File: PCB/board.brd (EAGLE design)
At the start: 160 x 100 mm, 24 parts, among them J1 DCJ0202, Q1 CRYSTAL_16MHZ_SMD, U1 MLX90614_

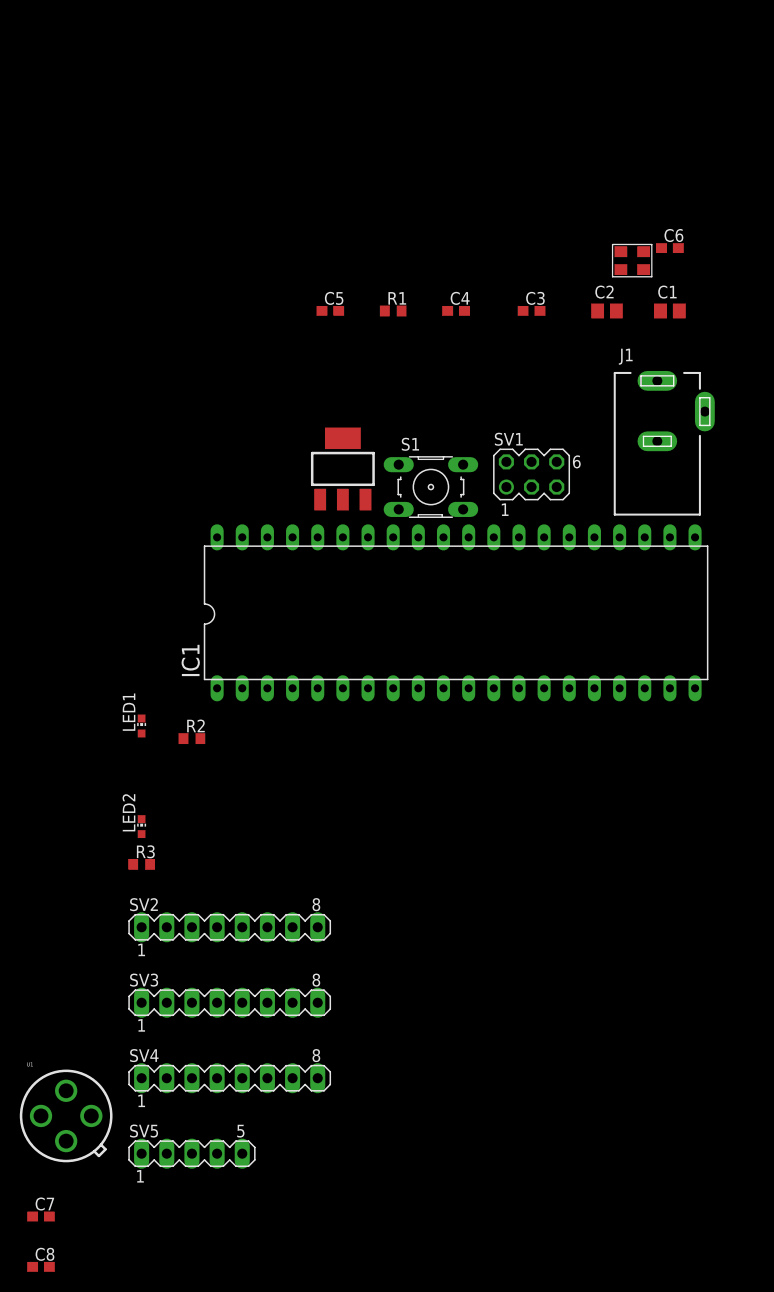
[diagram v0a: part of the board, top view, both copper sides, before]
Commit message: updated PCB with new LDO and PCB footprint
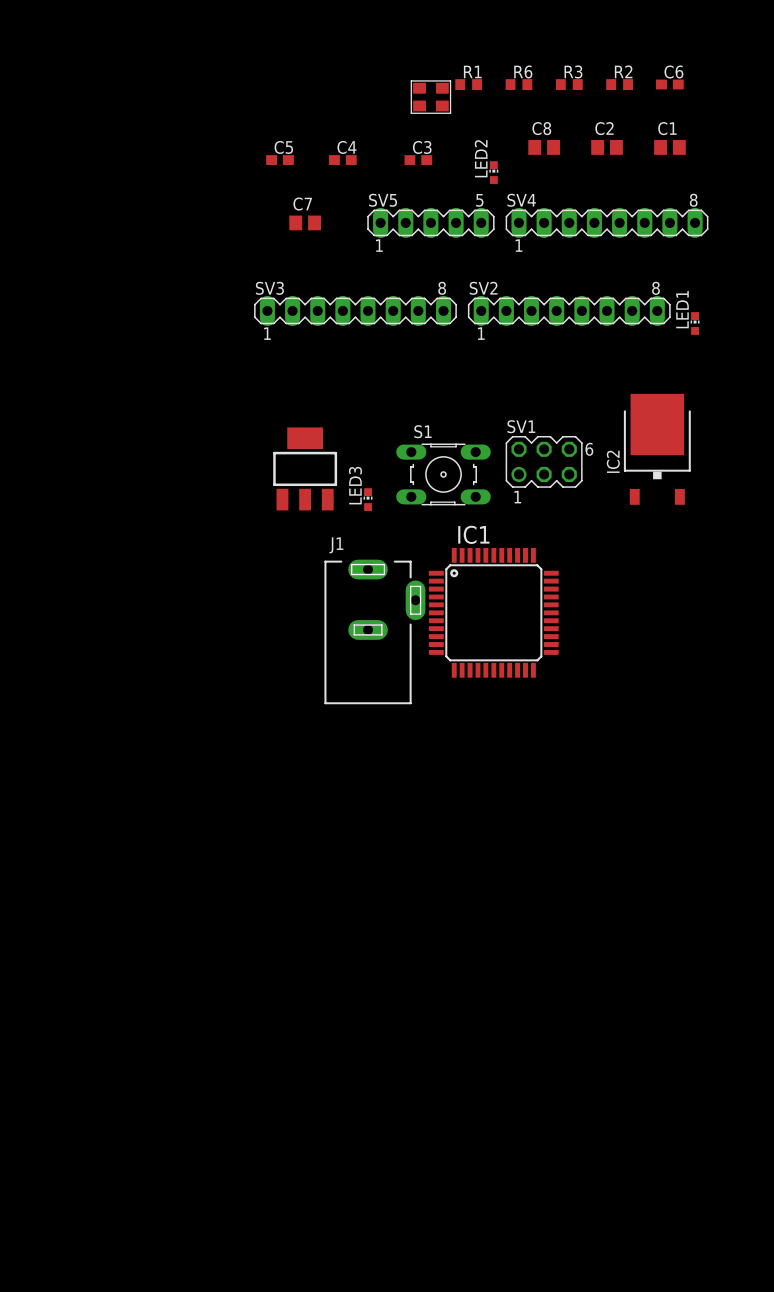
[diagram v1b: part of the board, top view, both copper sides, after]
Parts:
- removed U1: MLX90614_, SparkFun:TO-39
- added IC2: MC33269D-3.3, linear:DPACK
- added LED3: YELLOW, led:CHIP-LED0603
- added R6: 150, rcl:R0603
- C7: value 10pF -> 0.33uF; device rcl:C0603 -> rcl:C0805
- C8: value 10pF -> 10uF; device rcl:C0603 -> rcl:C0805
- IC1: value (none) -> MEGA1284P-SQUARE; device 1284p:DIL40 -> 1284p:TQFP44
- R1: value 10k Ohms -> 10k
- R2, R3: value 150 Ohms -> 150
- moved C8 123.9 mm to (-30.5, 57.1)
- moved C7 103.8 mm to (-54.6, 49.5)
- moved SV5 97.0 mm to (-41.9, 49.5)
- moved SV4 94.4 mm to (-24.1, 49.5)
- moved R3 89.8 mm to (-27.9, 63.5)
- moved R2 78.9 mm to (-22.9, 63.5)
- moved LED2 75.0 mm to (-35.6, 54.6)
- moved SV2 71.1 mm to (-27.9, 40.6)
- moved SV3 71.0 mm to (-49.5, 40.6)
- moved LED1 69.1 mm to (-15.2, 39.4)
- moved J1 34.9 mm to (-48.3, 11.4)
- moved Q1 26.2 mm to (-41.9, 62.2)
- moved R1 24.1 mm to (-38.1, 63.5)
- moved C3 19.1 mm to (-43.2, 55.9)
- moved C4 19.1 mm to (-50.8, 55.9)
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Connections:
- new net N$37: LED3.A, R6.1
- net +3V3: now also C8.1, IC2.2, R6.2; no longer U1.3
- net +5V: now also C7.1, IC1.27, IC1.5, IC2.3; no longer IC1.10, IC1.30
- net GND: now also C7.2, IC1.28, IC1.6, IC2.1, LED3.C; no longer C7.1, IC1.11, IC1.31, U1.4
- net MISO: now also IC1.2; no longer IC1.7
- net MOSI: now also IC1.1; no longer IC1.6
- net N$10: now also IC1.13; no longer IC1.18
- net N$11: now also IC1.12; no longer IC1.17
- net N$12: now also IC1.11; no longer IC1.16
- net N$13: now also IC1.10; no longer IC1.15
- net N$14: now also IC1.9; no longer IC1.14
- net N$15: now also IC1.26; no longer IC1.29
- net N$16: now also IC1.25; no longer IC1.28
- net N$17: now also IC1.24; no longer IC1.27
- net N$18: now also IC1.23; no longer IC1.26
- net N$19: now also IC1.22; no longer IC1.25
- net N$2: now also IC1.29; no longer IC1.32
- net N$20: now also IC1.21; no longer IC1.24
- net N$23: now also IC1.37; no longer IC1.40
- net N$24: now also IC1.36; no longer IC1.39
- net N$25: now also IC1.35; no longer IC1.38
- net N$26: now also IC1.34; no longer IC1.37
- net N$27: now also IC1.33; no longer IC1.36
- net N$28: now also IC1.32; no longer IC1.35
- net N$29: now also IC1.31; no longer IC1.34
- net N$3: now also IC1.8; no longer IC1.13
- net N$30: now also IC1.30; no longer IC1.33
- net N$31: now also IC1.40; no longer IC1.1
- net N$32: now also IC1.41; no longer IC1.2
- net N$33: now also IC1.42; no longer IC1.3
- net N$34: now also IC1.43; no longer IC1.4
- net N$35: now also IC1.44; no longer IC1.5
- net N$4: now also IC1.7; no longer IC1.12
- net N$7: now also IC1.16; no longer IC1.21
- net N$8: now also IC1.15; no longer IC1.20
- net N$9: now also IC1.14; no longer IC1.19
- net RESET: now also IC1.4; no longer IC1.9
- net SCK: now also IC1.3; no longer IC1.8
- net SCL: now also IC1.19; no longer C7.2, IC1.22, U1.1
- net SDA: now also IC1.20; no longer C8.1, IC1.23, U1.2
